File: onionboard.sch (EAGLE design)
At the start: 173 parts, among them IC1 IR4427S, IC2 IR4427S, J1 22-27-2041-04, Q1 FDD4141TO252, Q2 FDD4141TO252, Q3 FDD4141TO252, Q4 FDD4141TO252, Q5 FDD4141TO252, Q6 FDD4141TO252, X1 5569-8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

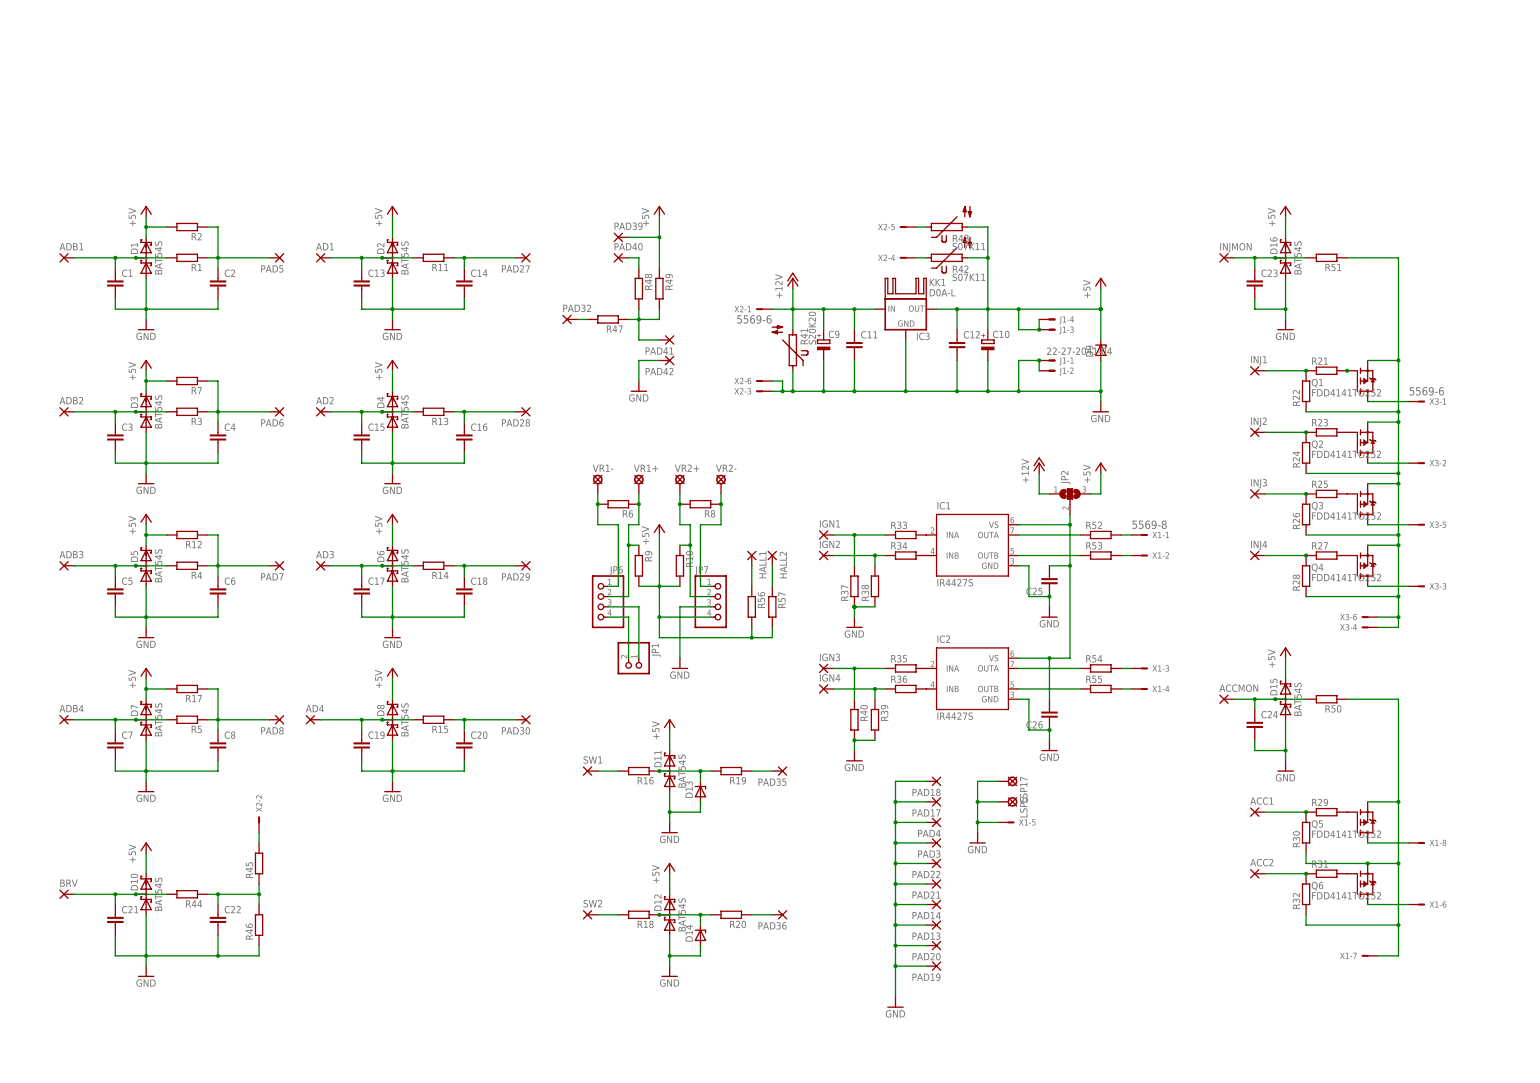
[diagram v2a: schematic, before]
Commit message: Even more schematic refactor and added values to components. Added silkscreen for molex connectors
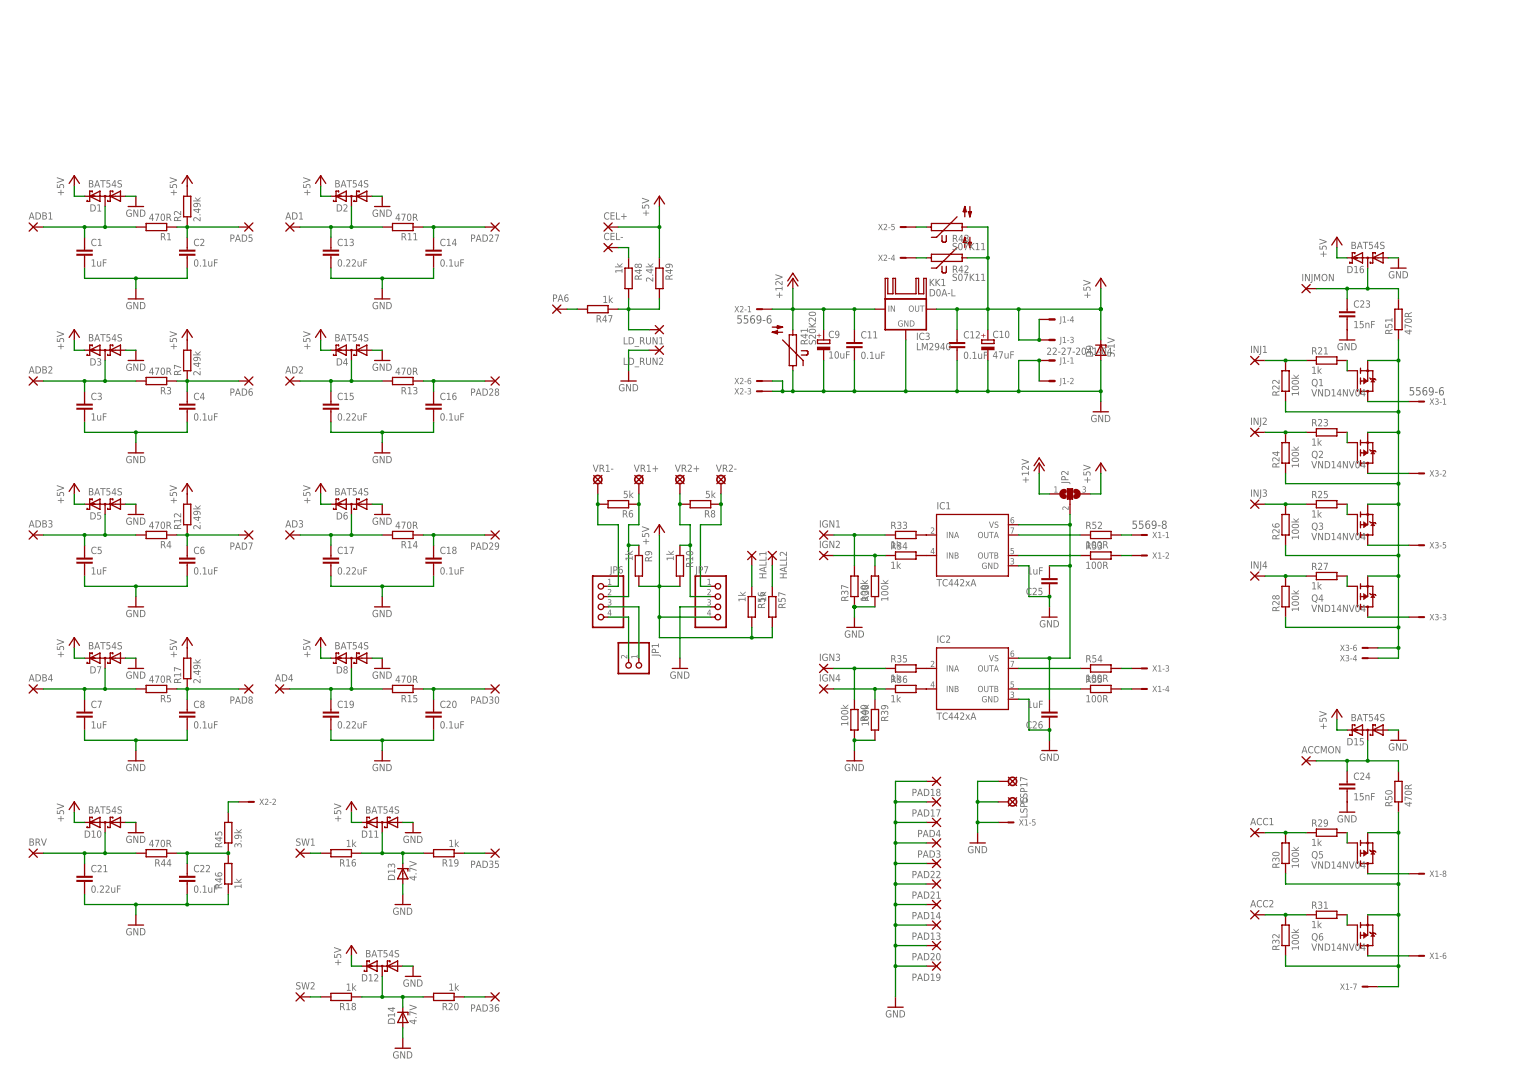
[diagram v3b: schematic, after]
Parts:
- removed PAD32, PAD39, PAD40, PAD41, PAD42: (no value), wirepad:SMD2
- added CEL+, CEL-, LD_RUN1, LD_RUN2, PA6: (no value), wirepad:SMD2
- C1, C25, C26, C3, C5, C7: value (none) -> 1uF
- C10: value (none) -> 47uF
- C11, C12, C14, C16, C18, C2, C20, C22, C4, C6, C8: value (none) -> 0.1uF
- C13, C15, C17, C19, C21: value (none) -> 0.22uF
- C23, C24: value (none) -> 15nF
- C9: value (none) -> 10uF
- D13, D14: value (none) -> 4.7V
- D9: value (none) -> 5.1V
- IC1, IC2: value IR4427S -> TC442xA
- IC3: value (none) -> LM2940
- Q1, Q2, Q3, Q4, Q5, Q6: value FDD4141TO252 -> VND14NV04
- R1, R11, R13, R14, R15, R3, R4, R44, R5, R50, R51: value (none) -> 470R
- R10, R16, R18, R19, R20, R21, R23, R25, R27, R29, R31, R33, R34, R35, R36, R46, R47, R48, R56, R57, R9: value (none) -> 1k
- R12, R17, R2, R7: value (none) -> 2.49k
- R22, R24, R26, R28, R30, R32, R37, R38, R39, R40: value (none) -> 100k
- R45: value (none) -> 3.9k
- R49: value (none) -> 2.4k
- R52, R53, R54, R55: value (none) -> 100R
- R6, R8: value (none) -> 5k
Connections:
- net +5V: now also CEL+.P; no longer PAD39.P
- net GND: now also LD_RUN2.P; no longer PAD42.P
- net N$24: now also PA6.P; no longer PAD32.P
- net N$81: now also LD_RUN1.P; no longer PAD41.P
- net N$86: now also CEL-.P; no longer PAD40.P
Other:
- moved on the sheet: ACC1, ACC2, ACCMON, AD1, AD2, AD3, AD4, ADB1, ADB2, ADB3, ADB4, BRV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

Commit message: Added git commit id to schematic and added the filter into gitattributes. Also updated README with the commit id filter info
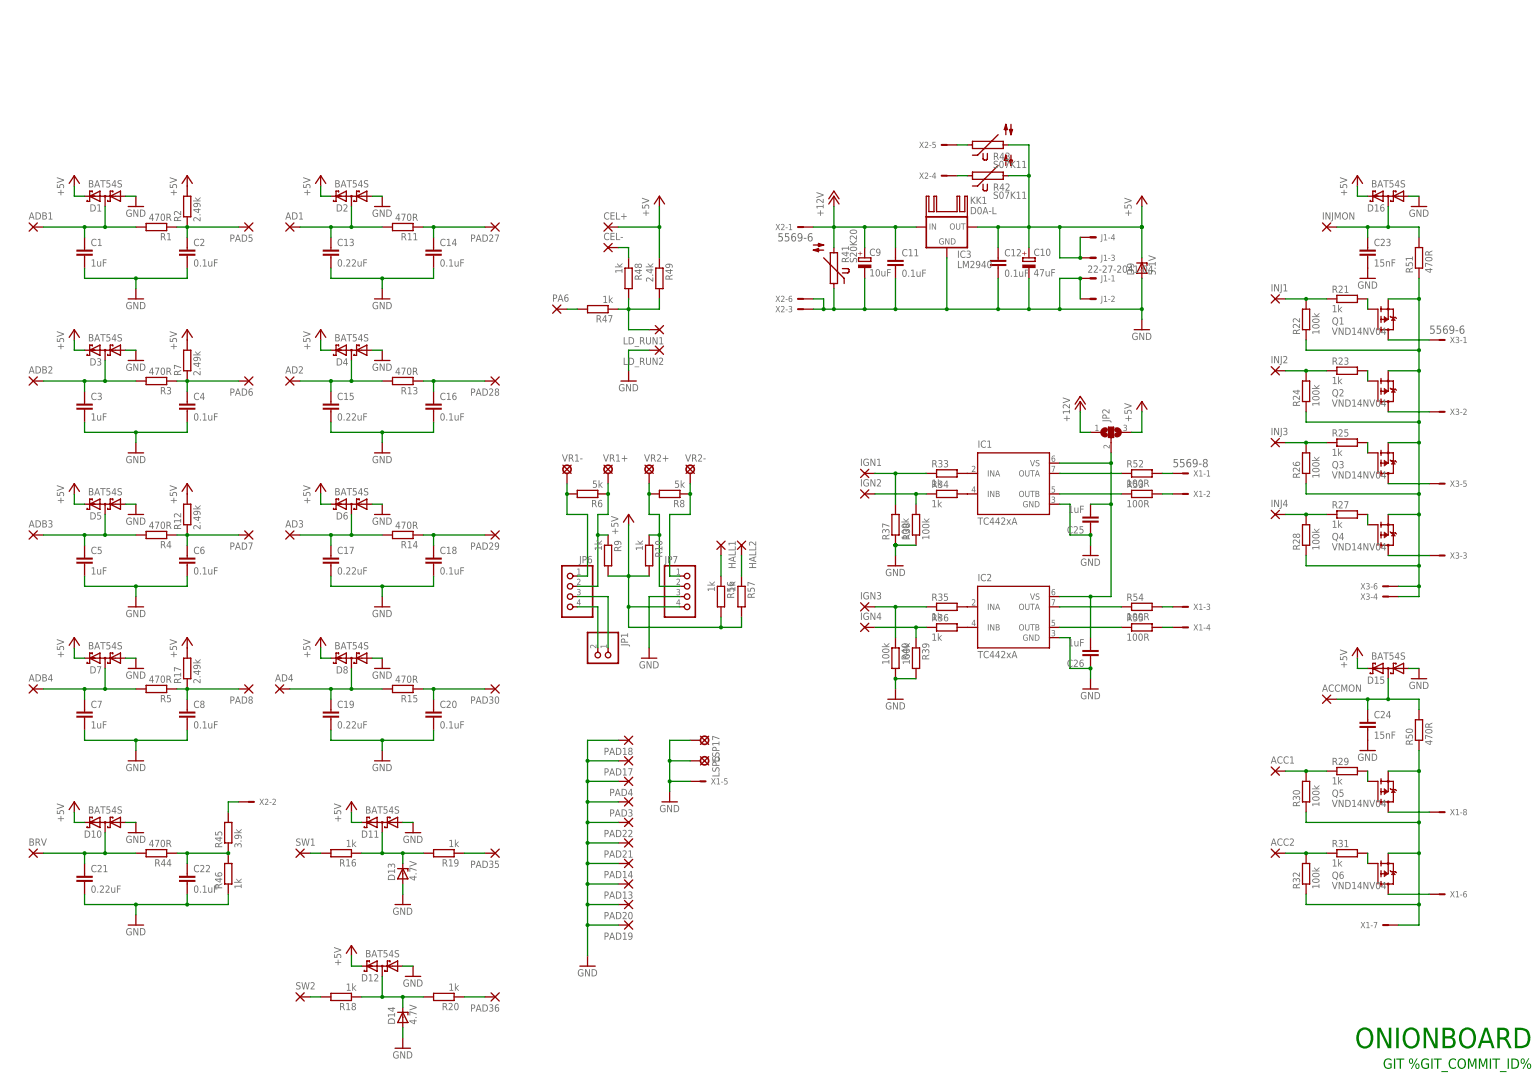
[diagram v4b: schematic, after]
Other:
- note added: "GIT %GIT_COMMIT_ID%"
- note added: "ONIONBOARD"
- moved on the sheet: ACC1, ACC2, ACCMON, C10, C11, C12, C23, C24, C25, C26, C9, D15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

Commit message: Changed VDR/MOV size from 20mm to 14mm. Moved powersupply section a bit lower to fit the heatsink properly
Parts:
- R41: value S20K20 -> S14K11; device varistor:S20K20 -> varistor:S14K11
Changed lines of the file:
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@@
 <part name="R39" library="resistor" deviceset="R-EU_" device="M0805" value="100k"/>
 <part name="R40" library="resistor" deviceset="R-EU_" device="M0805" value="100k"/>
-<part name="R41" library="varistor" deviceset="S20K20" device=""/>
+<part name="R41" library="varistor" deviceset="S14K11" device=""/>
 <part name="R42" library="varistor" deviceset="S07K11" device=""/>
 <part name="R43" library="varistor" deviceset="S07K11" device=""/>
